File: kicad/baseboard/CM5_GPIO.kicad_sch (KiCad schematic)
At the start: 18 parts, among them J11 Conn_01x02_Pin, J14 JST_SHBM04B-SRSS-TB, J3 Conn_01x02_Pin, J8 THD-20-R, SW1 SW_SPST, U1 TPD4EUSB30, U2 TPD4EUSB30, U3 MagJack-A70-112-331N126, U9 L7805

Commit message: Finish PCB routing
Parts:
- D1: footprint LED_SMD:LED_0603_1608Metric -> LED_SMD:LED_0805_2012Metric; LCSC Part # C2286 -> C84256
- D2: footprint LED_SMD:LED_0603_1608Metric -> LED_SMD:LED_0805_2012Metric
- U3: LCSC Part # (none) -> C9900132877; j C9900132877 -> (none)
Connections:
- net BAT AD IN: no longer names the net of J11.2 (Pin_2), SW1.2 (B)
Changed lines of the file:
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@@
 	)
 	(junction
+		(at 128.27 118.11)
+		(diameter 0)
+		(color 0 0 0 0)
+	)
+	(junction
 		(at 101.6 95.25)
 		(diameter 1.016)
@@
 	)
 	(junction
-		(at 115.57 118.11)
-		(diameter 0)
-		(color 0 0 0 0)
-	)
-	(junction
 		(at 190.5 123.19)
 		(diameter 0)
@@
 	)
 	(junction
-		(at 147.32 177.8)
-		(diameter 0)
-		(color 0 0 0 0)
-	)
-	(junction
 		(at 149.86 24.13)
 		(diameter 1.016)
@@
 	(wire
 		(pts
-			(xy 100.33 118.11) (xy 115.57 118.11)
-		)
-		(stroke
-			(width 0)
-			(type solid)
-		)
-	)
-	(wire
-		(pts
 			(xy 101.6 36.83) (xy 101.6 49.53)
 		)
@@
 	(wire
 		(pts
+			(xy 128.27 118.11) (xy 129.54 118.11)
+		)
+		(stroke
+			(width 0)
+			(type solid)
+		)
+	)
+	(wire
+		(pts
 			(xy 104.14 133.35) (xy 118.11 133.35)
 		)
@@
 	(wire
 		(pts
-			(xy 147.32 177.8) (xy 148.59 177.8)
+			(xy 137.16 177.8) (xy 148.59 177.8)
 		)
 		(stroke
@@
 	(wire
 		(pts
+			(xy 128.27 118.11) (xy 128.27 123.19)
+		)
+		(stroke
+			(width 0)
+			(type default)
+		)
+	)
+	(wire
+		(pts
 			(xy 100.33 120.65) (xy 100.33 123.19)
 		)
@@
 	(wire
 		(pts
-			(xy 115.57 118.11) (xy 129.54 118.11)
-		)
-		(stroke
-			(width 0)
-			(type solid)
-		)
-	)
-	(wire
-		(pts
 			(xy 100.33 52.07) (xy 114.3 52.07)
 		)
@@
 	(wire
 		(pts
-			(xy 115.57 119.38) (xy 115.57 118.11)
-		)
-		(stroke
-			(width 0)
-			(type solid)
-		)
-	)
-	(wire
-		(pts
 			(xy 25.4 123.19) (xy 39.37 123.19)
 		)
@@
 	(wire
 		(pts
-			(xy 147.32 177.8) (xy 147.32 170.18)
-		)
-		(stroke
-			(width 0)
-			(type default)
-		)
-	)
-	(wire
-		(pts
 			(xy 100.33 64.77) (xy 114.3 64.77)
 		)
@@
 	(wire
 		(pts
-			(xy 137.16 177.8) (xy 147.32 177.8)
-		)
-		(stroke
-			(width 0)
-			(type default)
-		)
-	)
-	(wire
-		(pts
 			(xy 165.1 31.75) (xy 176.53 31.75)
 		)
@@
 	(wire
 		(pts
+			(xy 200.66 120.65) (xy 204.47 120.65)
+		)
+		(stroke
+			(width 0)
+			(type default)
+		)
+	)
+	(wire
+		(pts
 			(xy 24.13 62.23) (xy 39.37 62.23)
 		)
@@
 	(wire
 		(pts
+			(xy 100.33 118.11) (xy 128.27 118.11)
+		)
+		(stroke
+			(width 0)
+			(type solid)
+		)
+	)
+	(wire
+		(pts
 			(xy 148.59 129.54) (xy 160.02 129.54)
 		)
@@
 	(wire
 		(pts
-			(xy 193.04 120.65) (xy 204.47 120.65)
-		)
-		(stroke
-			(width 0)
-			(type solid)
-		)
-	)
-	(wire
-		(pts
 			(xy 38.1 85.09) (xy 39.37 85.09)
 		)
@@
 		)
 	)
-	(label "BAT AD IN"
-		(at 147.32 170.18 180)
-		(effects
-			(font
-				(size 1.27 1.27)
-			)
-			(justify right bottom)
-		)
-	)
-	(label "+5v"
-		(at 194.31 120.65 0)
-		(effects
-			(font
-				(size 1.27 1.27)
-			)
-			(justify left bottom)
-		)
-	)
 	(label "+3.3v"
 		(at 190.5 105.41 180)
@@
 		)
 	)
+	(global_label "+5v"
+		(shape input)
+		(at 128.27 123.19 0)
+		(fields_autoplaced yes)
+		(effects
+			(font
+				(size 1.27 1.27)
+			)
+			(justify left)
+		)
+		(property "Intersheetrefs" "${INTERSHEET_REFS}"
+			(at 135.0998 123.19 0)
+			(effects
+				(font
+					(size 1.27 1.27)
+				)
+				(justify left)
+				(hide yes)
+			)
+		)
+	)
 	(global_label "BatterieSwitch"
 		(shape input)
@@
 		)
 	)
+	(global_label "+5v"
+		(shape input)
+		(at 200.66 120.65 180)
+		(fields_autoplaced yes)
+		(effects
+			(font
+				(size 1.27 1.27)
+			)
+			(justify right)
+		)
+		(property "Intersheetrefs" "${INTERSHEET_REFS}"
+			(at 193.8302 120.65 0)
+			(effects
+				(font
+					(size 1.27 1.27)
+				)
+				(justify right)
+				(hide yes)
+			)
+		)
+	)
 	(global_label "BatterieSwitch"
 		(shape input)
@@
 		)
 	)
-	(hierarchical_label "+5v"
-		(shape input)
-		(at 115.57 119.38 0)
-		(effects
-			(font
-				(size 1.27 1.27)
-			)
-			(justify left)
-		)
-	)
 	(symbol
 		(lib_id "CM5IO:ComputeModule5-CM5")
@@
 			)
 		)
-		(property "Footprint" "LED_SMD:LED_0603_1608Metric"
+		(property "Footprint" "LED_SMD:LED_0805_2012Metric"
 			(at 116.84 27.94 0)
 			(effects
@@
 			)
 		)
-		(property "Footprint" "LED_SMD:LED_0603_1608Metric"
+		(property "Footprint" "LED_SMD:LED_0805_2012Metric"
 			(at 160.02 113.03 0)
 			(effects
@@
 			)
 		)
-		(property "LCSC Part #" "C2286"
+		(property "LCSC Part #" "C84256"
 			(at 160.02 113.03 90)
 			(effects
@@
 			)
 		)
-		(property "j" "C9900132877"
+		(property "LCSC Part #" "C9900132877"
 			(at 267.97 92.71 0)
 			(effects

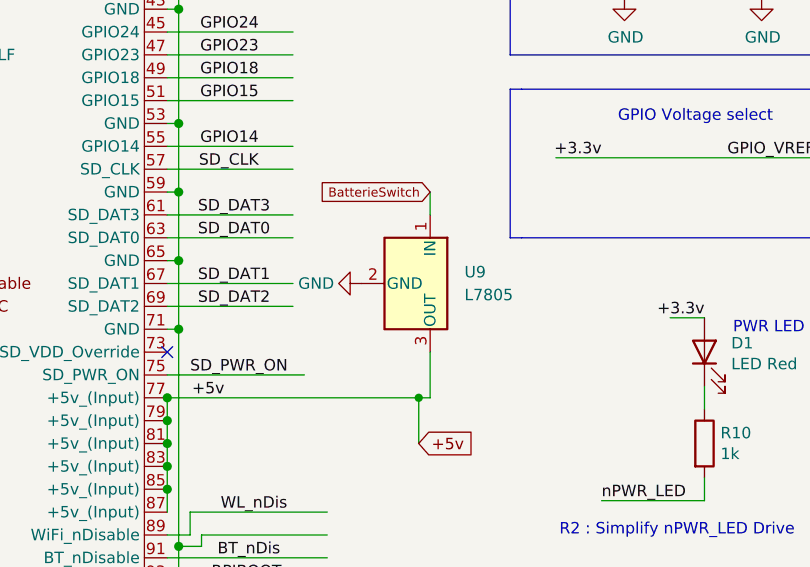
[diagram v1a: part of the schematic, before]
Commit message: Setup baseboard pcb production settings
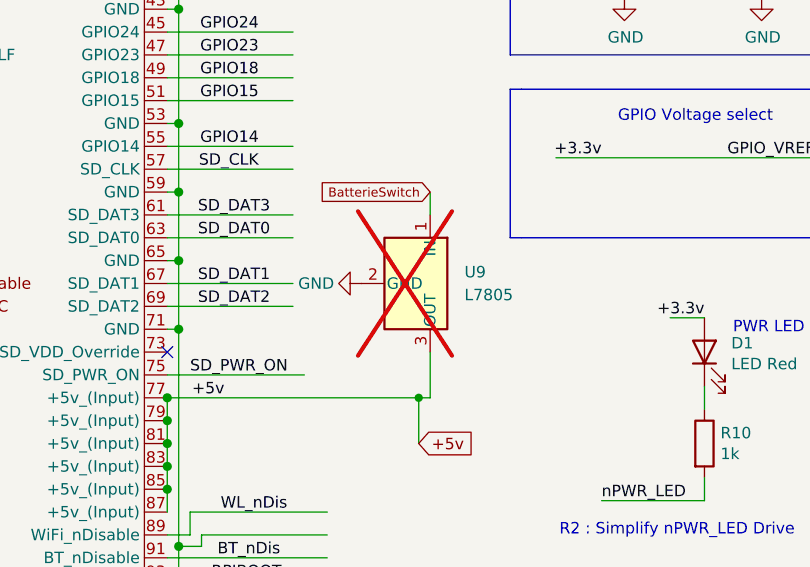
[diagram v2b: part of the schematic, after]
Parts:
- U3: LCSC Part # C9900132877 -> C22457393
- U9: now not fitted
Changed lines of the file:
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@@
 		(in_bom yes)
 		(on_board yes)
-		(dnp no)
+		(dnp yes)
 		(fields_autoplaced yes)
 		(property "Reference" "U9"
@@
 			)
 		)
-		(property "LCSC Part #" "C9900132877"
-			(at 267.97 92.71 0)
-			(effects
+		(property "LCSC Part #" "C22457393"
+			(at 267.97 92.71 0)
+			(effects

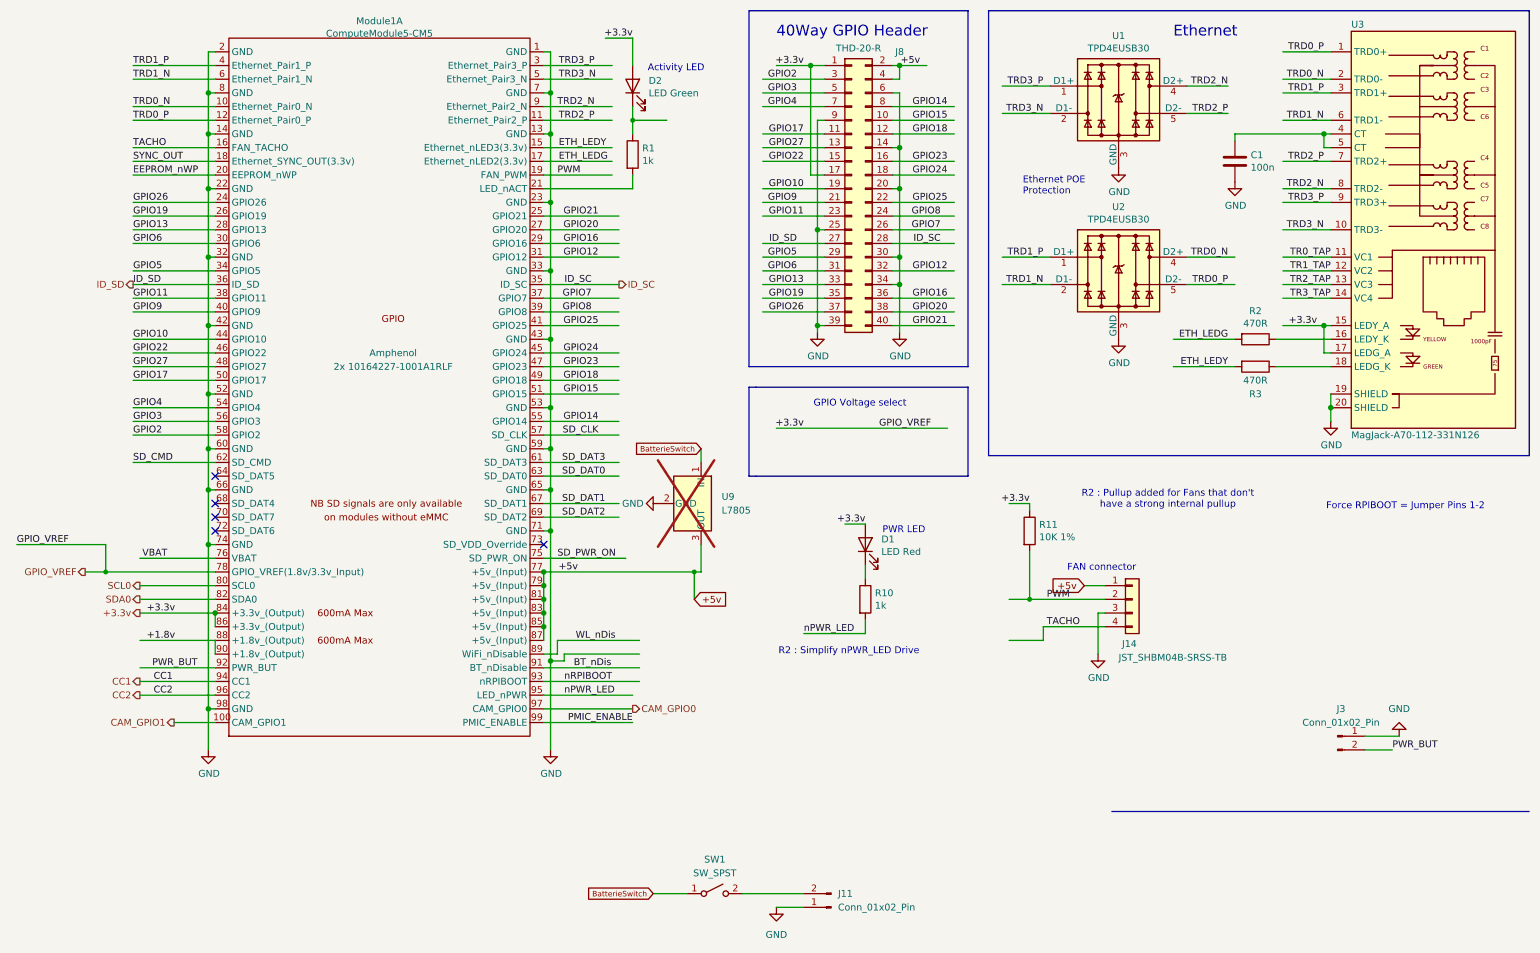
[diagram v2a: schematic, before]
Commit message: Correct V1 mistakes : Turned MISO, Correct STM32 template.   Add BMO055 Gyroskope . Add servo connector. Add serial port connector. Add Pi - Stm32 serial connection. Add Silkscreen texts.
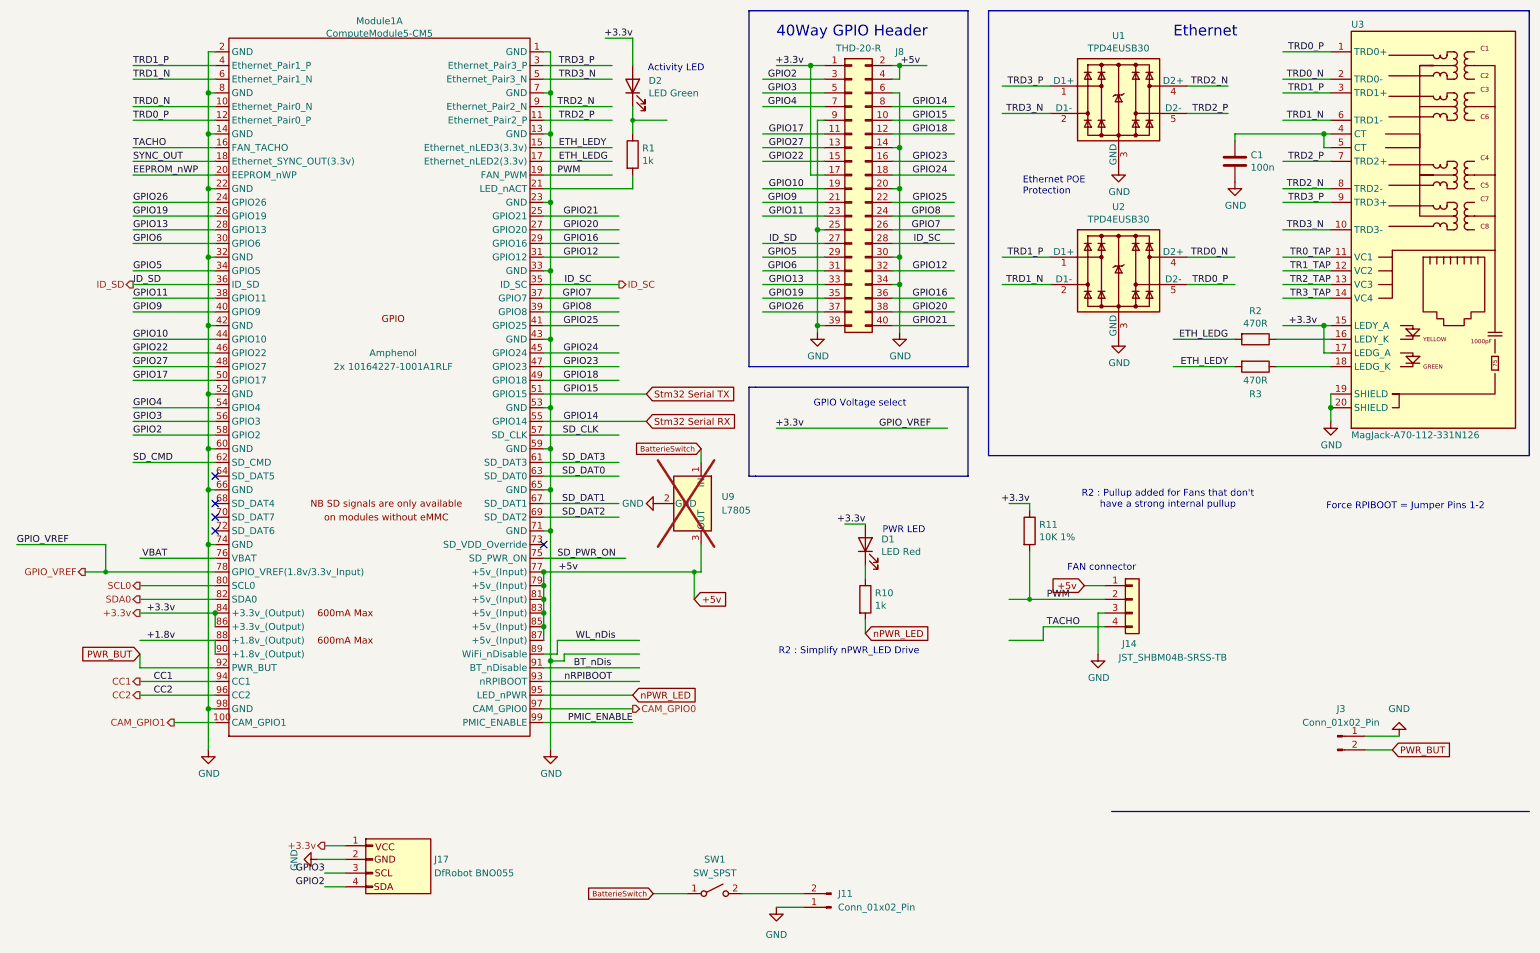
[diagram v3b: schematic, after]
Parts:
- added J17: DfRobot BNO055, WroStuff:DfRobot BNO055, symbol wrostuff:BNO055_Modul
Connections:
- net +3.3v: now also J17.1 (VCC_33)
- net GND: now also J17.2 (GND)
- net GPIO2: now also J17.4 (SDA)
- net GPIO3: now also J17.3 (SCL)
- net GPIO14 renamed Stm32 Serial RX
- net GPIO15 renamed Stm32 Serial TX
